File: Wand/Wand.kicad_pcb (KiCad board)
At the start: 4 copper layers, 50 x 7 mm, 20 parts, among them P1 ISP, P2 KLB4, P3 BASE, U1 ATMEGA328-MMH, U2 MAX31855KASA+, U3 MPU-6050

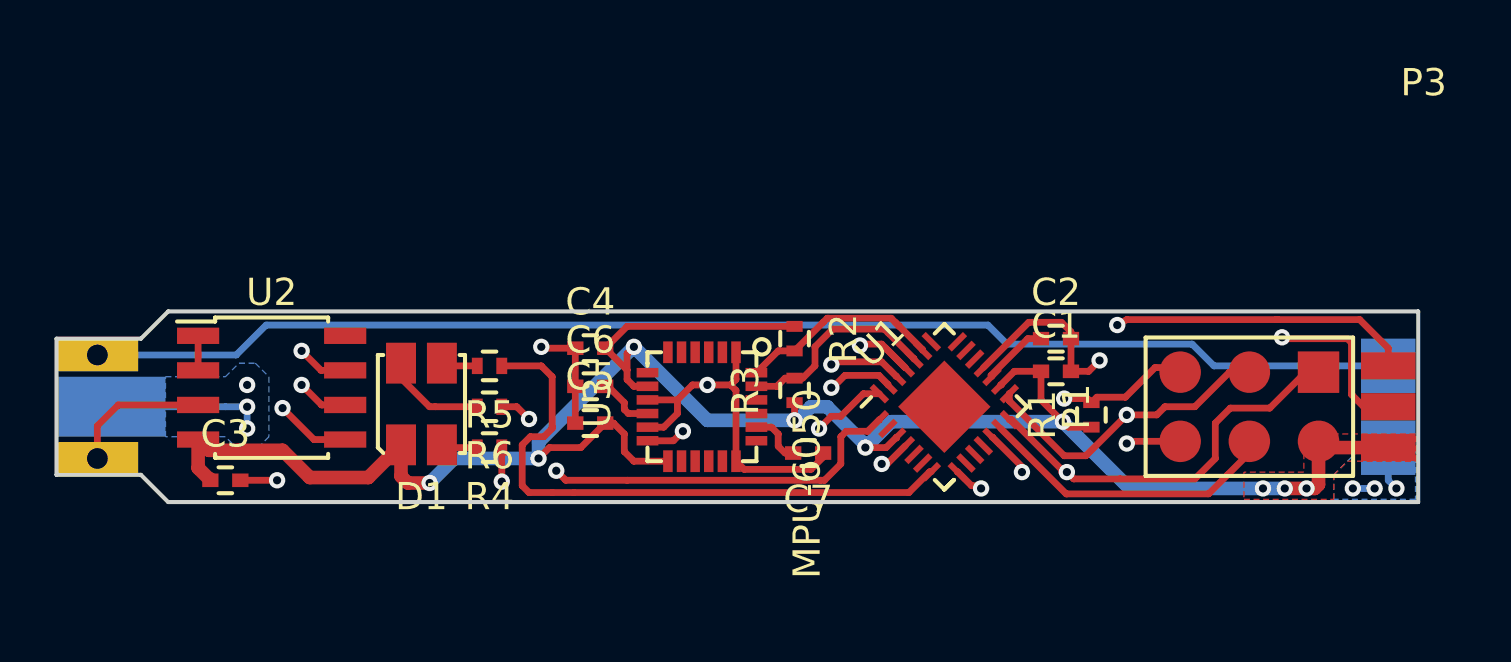
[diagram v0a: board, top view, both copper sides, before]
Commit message: Sorted out the trace for the tip power and finalised the rest of the layout for review
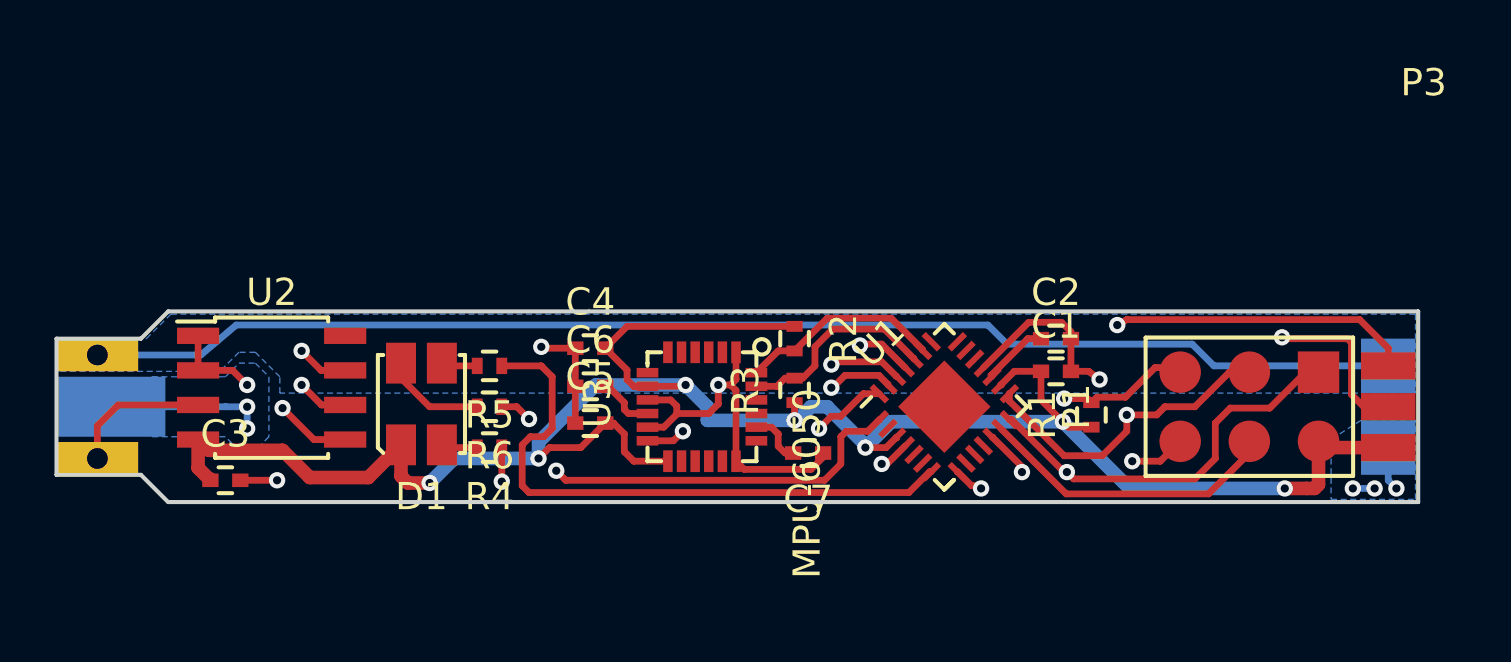
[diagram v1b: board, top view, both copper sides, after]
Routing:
- net GND: track 90.7 -> 93.7 mm
- net /RESET: track 21.5 -> 20.4 mm
- net +3V3: vias 9 -> 7
- added copper zone on B.Cu, net /HEAT
- removed copper zone on F.Cu, net +3V3

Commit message: Slight tweak to allow more copper for tip power rail
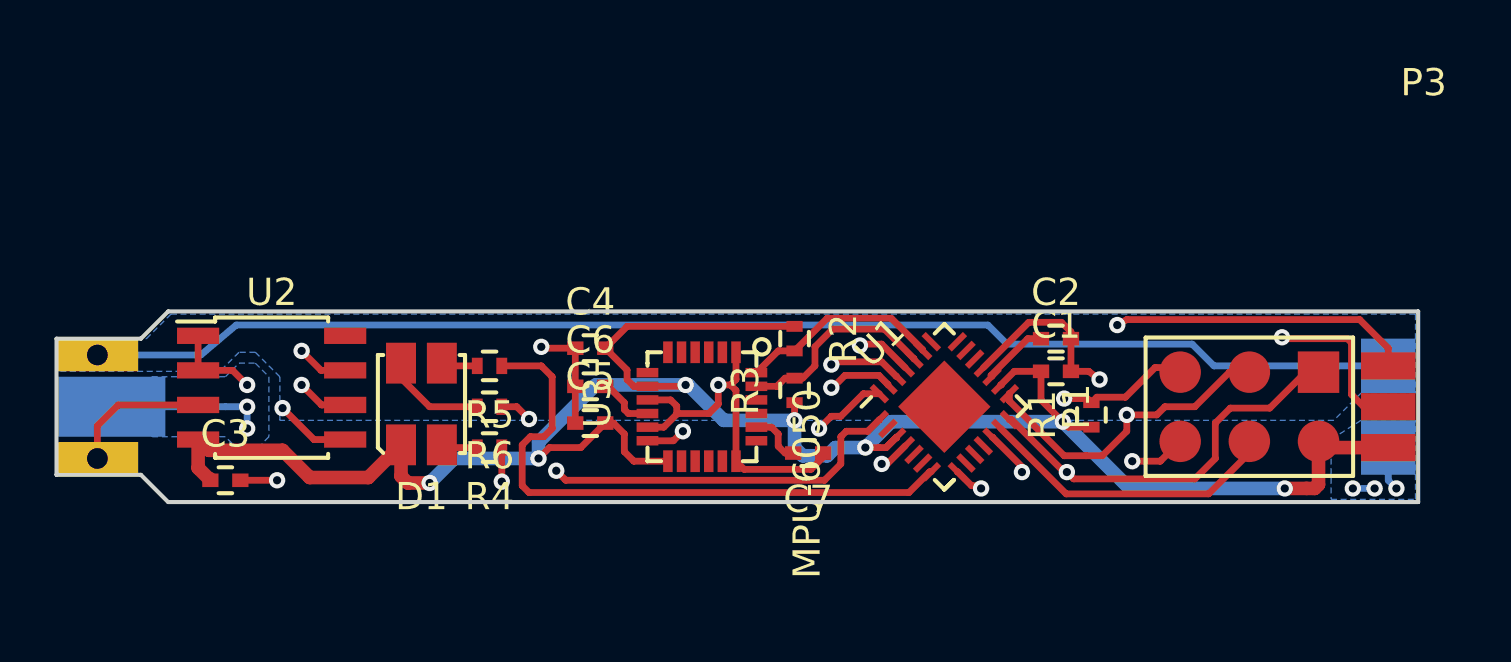
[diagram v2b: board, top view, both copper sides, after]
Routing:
- net +3V3: track 80.3 -> 80.9 mm
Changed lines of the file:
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@@
     (links 57)
     (no_connects 0)
-    (area 83.414287 99.025 161.985715 132.377185)
+    (area 96.924999 108.424999 147.075001 115.575001)
     (thickness 1.6)
     (drawings 14)
-    (tracks 366)
+    (tracks 368)
     (zones 0)
     (modules 20)
@@
   (layers
     (0 F.Signal.Cu signal)
-    (1 In1.Ground.Cu power)
-    (2 In2.Signal.Cu signal)
-    (31 B.Power.Cu mixed)
+    (1 In1.Ground.Cu power hide)
+    (2 In2.Signal.Cu signal hide)
+    (31 B.Power.Cu mixed hide)
     (32 B.Adhes user)
     (33 F.Adhes user)
@@
     (arrow2b (pts (xy 93.800001 109.5) (xy 94.386422 110.626504)))
   )
+  (segment (start 126.7 113.5) (end 125.6 113.5) (width 0.5) (layer B.Power.Cu) (net 1))
+  (segment (start 124.1 113.5) (end 124.1 112.5) (width 0.5) (layer B.Power.Cu) (net 1))
+  (segment (start 124.4 113.8) (end 124.1 113.5) (width 0.5) (layer B.Power.Cu) (net 1))
+  (segment (start 125.3 113.8) (end 124.4 113.8) (width 0.5) (layer B.Power.Cu) (net 1))
+  (segment (start 125.6 113.5) (end 125.3 113.8) (width 0.5) (layer B.Power.Cu) (net 1))
+  (segment (start 127.65 112.55) (end 126.7 113.5) (width 0.5) (layer B.Power.Cu) (net 1))
+  (segment (start 133.95 112.55) (end 127.65 112.55) (width 0.5) (layer B.Power.Cu) (net 1))
+  (segment (start 126.7 113.5) (end 127.2 113.5) (width 0.25) (layer F.Signal.Cu) (net 1))
+  (via (at 126.7 113.5) (size 0.6) (drill 0.3) (layers F.Signal.Cu B.Power.Cu) (net 1))
+  (segment (start 127.2 113.5) (end 127.463604 113.5) (width 0.25) (layer F.Signal.Cu) (net 1))
+  (segment (start 127.463604 113.5) (end 127.849911 113.113693) (width 0.25) (layer F.Signal.Cu) (net 1))
+  (segment (start 127.463604 113.5) (end 127.849911 113.113693) (width 0.25) (layer F.Signal.Cu) (net 1) (status 20))
+  (segment (start 120.1 111.2) (end 120.2 111.2) (width 0.5) (layer B.Power.Cu) (net 1))
+  (segment (start 120.2 111.2) (end 121.5 112.5) (width 0.5) (layer B.Power.Cu) (net 1))
+  (segment (start 121.5 112.5) (end 124.1 112.5) (width 0.5) (layer B.Power.Cu) (net 1))
   (segment (start 142.9 115) (end 142.1 115) (width 0.5) (layer F.Signal.Cu) (net 1))
   (via (at 142.1 115) (size 0.6) (drill 0.3) (layers F.Signal.Cu B.Power.Cu) (net 1))
@@
   (segment (start 116.8 111.2) (end 114.7 113.3) (width 0.5) (layer B.Power.Cu) (net 1))
   (segment (start 118.2 111.25) (end 120.05 111.25) (width 0.25) (layer F.Signal.Cu) (net 1))
-  (segment (start 120.9 112) (end 120.1 111.2) (width 0.5) (layer B.Power.Cu) (net 1))
   (via (at 120.1 111.2) (size 0.6) (drill 0.3) (layers F.Signal.Cu B.Power.Cu) (net 1))
-  (segment (start 120.9 112.5) (end 124.1 112.5) (width 0.5) (layer B.Power.Cu) (net 1))
-  (segment (start 120.9 112.5) (end 120.9 112) (width 0.5) (layer B.Power.Cu) (net 1))
   (segment (start 120.05 111.25) (end 120.1 111.2) (width 0.25) (layer F.Signal.Cu) (net 1))
-  (segment (start 133.95 112.55) (end 127.65 112.55) (width 0.5) (layer B.Power.Cu) (net 1))
-  (segment (start 127.65 112.55) (end 126.7 113.5) (width 0.5) (layer B.Power.Cu) (net 1))
-  (segment (start 124.1 112.5) (end 124.2 112.5) (width 0.5) (layer B.Power.Cu) (net 1))
-  (segment (start 126.7 113.4) (end 126.7 113.5) (width 0.5) (layer B.Power.Cu) (net 1))
-  (segment (start 125.3 112) (end 126.7 113.4) (width 0.5) (layer B.Power.Cu) (net 1))
-  (segment (start 124.7 112) (end 125.3 112) (width 0.5) (layer B.Power.Cu) (net 1))
-  (segment (start 124.2 112.5) (end 124.7 112) (width 0.5) (layer B.Power.Cu) (net 1))
   (via (at 124.1 112.5) (size 0.6) (drill 0.3) (layers F.Signal.Cu B.Power.Cu) (net 1))
   (segment (start 124.1 112.5) (end 124.1 111.85) (width 0.25) (layer F.Signal.Cu) (net 1) (status 20))
@@
   (segment (start 132.172792 110.7) (end 131.668287 111.204505) (width 0.25) (layer F.Signal.Cu) (net 1) (status 20))
   (segment (start 131.668287 111.204505) (end 131.695495 111.204505) (width 0.25) (layer F.Signal.Cu) (net 1) (status 30))
-  (segment (start 127.463604 113.5) (end 127.849911 113.113693) (width 0.25) (layer F.Signal.Cu) (net 1) (status 20))
-  (segment (start 126.7 113.5) (end 127.463604 113.5) (width 0.25) (layer F.Signal.Cu) (net 1))
-  (via (at 126.7 113.5) (size 0.6) (drill 0.3) (layers F.Signal.Cu B.Power.Cu) (net 1))
   (segment (start 127.849911 113.113693) (end 127.849911 113.150089) (width 0.25) (layer F.Signal.Cu) (net 1) (status 30))
   (segment (start 124.1 109.05) (end 117.95 109.05) (width 0.25) (layer F.Signal.Cu) (net 1) (status 10))
@@
     (polygon
       (pts
-        (xy 146.9 111.5) (xy 127.6 111.5) (xy 105.2 111.5) (xy 105.2 110.9) (xy 104.3 110)
-        (xy 103.7 110) (xy 103.2 110.5) (xy 103 110.7) (xy 97.1 110.7) (xy 97.1 109.5)
-        (xy 100.3 109.5) (xy 101.2 108.6) (xy 146.9 108.6)
+        (xy 146.9 111.5) (xy 144.9 111.5) (xy 143.9 112.5) (xy 127.6 112.5) (xy 105.2 112.5)
+        (xy 105.2 110.9) (xy 104.3 110) (xy 103.7 110) (xy 103.2 110.5) (xy 103 110.7)
+        (xy 97.1 110.7) (xy 97.1 109.5) (xy 100.3 109.5) (xy 101.2 108.6) (xy 146.9 108.6)
       )
     )
